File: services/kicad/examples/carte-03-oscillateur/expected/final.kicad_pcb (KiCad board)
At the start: 2 copper layers, 26 x 20 mm, 15 parts, among them J1 PWR, J2 OUT, U1 NE555

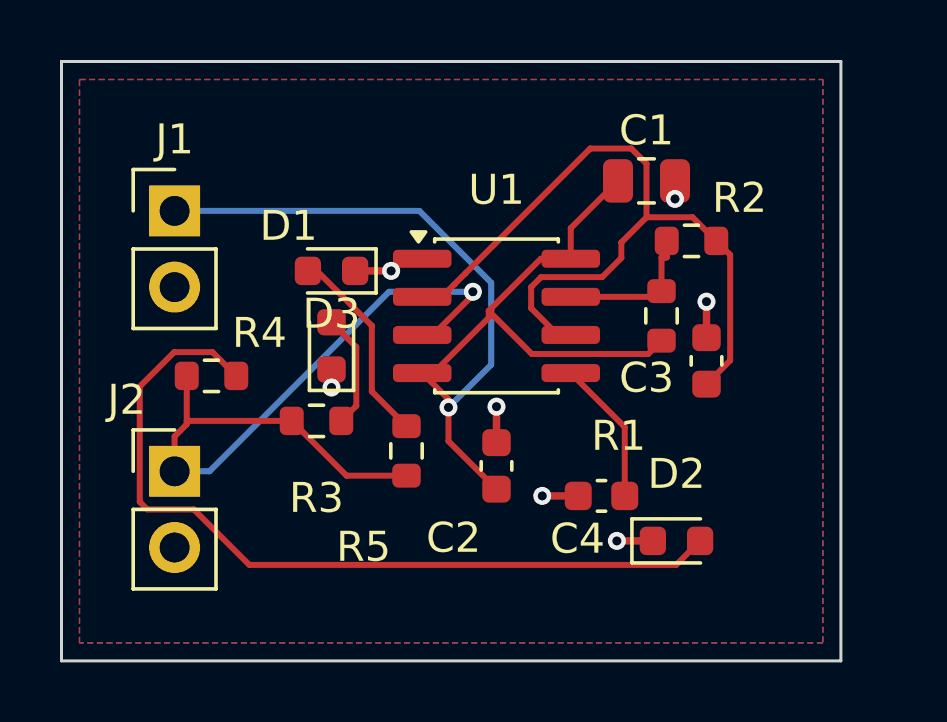
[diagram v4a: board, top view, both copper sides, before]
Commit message: feat(placement): les peripheriques se REPARTISSENT, ils ne s empilent plus
Question de l utilisateur devant le rendu : « c est quoi ce type de placement ? ».
Les composants s entassaient d un seul cote du boitier, etiquettes de
serigraphie l une sur l autre, trois quarts de la couronne vides.

TROIS CAUSES, toutes dans `_poser_les_peripheriques`, toutes la meme faute —
un angle unique pour tout un groupe :

  - les DIRECTS qui visent la meme broche (tous les decouplages d un rail,
    toutes les resistances d un meme signal) recevaient le MEME `angle_vers`
    et le meme rayon de depart ;
  - les SUIVEURS d un meme parent recevaient tous atan2(parent - centre) ;
  - les ISOLES partaient tous de l angle 0.0, c est-a-dire du meme point.

`le_long_du_rayon` ne s ecartait qu une fois la place prise : d ou la file.

REMEDE : `_ecart_en_eventail`. Le PREMIER de chaque groupe garde EXACTEMENT la
direction calculee — c est la topologie, on ne la perd pas pour faire joli — et
les suivants s ecartent symetriquement de 3 x `_PAS_ANGLE_DEG`.
Rien de deja pose ne bouge : seul l ANGLE DE DEPART de la recherche change, et
`le_long_du_rayon` reste seul juge de ce qui est libre.

BANC DES DIX CARTES, contour resserre ET peripheriques repartis :

    carte             demandee    livree         err  manq
    carte-01           25 x 20    20,1 x 13,6     0    0
    carte-02           55 x 40    34,9 x 25,2     0    0
    carte-03           50 x 35    27,6 x 19,9     0    0
    carte-04           60 x 45    36,6 x 29,8     0    0
    carte-05           70 x 50    40,0 x 32,6     0    0
    carte-06           80 x 60    46,5 x 36,4     0    0
    carte-07          110 x 80    47,7 x 38,8     0    0
    carte-08          125 x 95    57,4 x 44,1     0    0
    carte-09          130 x 100   57,8 x 45,2     0    0
    carte-10          140 x 105   59,0 x 45,8     0    0

Dix sur dix, 100 % route. carte-07 gagne 5,5 mm de largeur sur le passage
precedent, carte-06 deux, carte-10 deux. Sur ca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
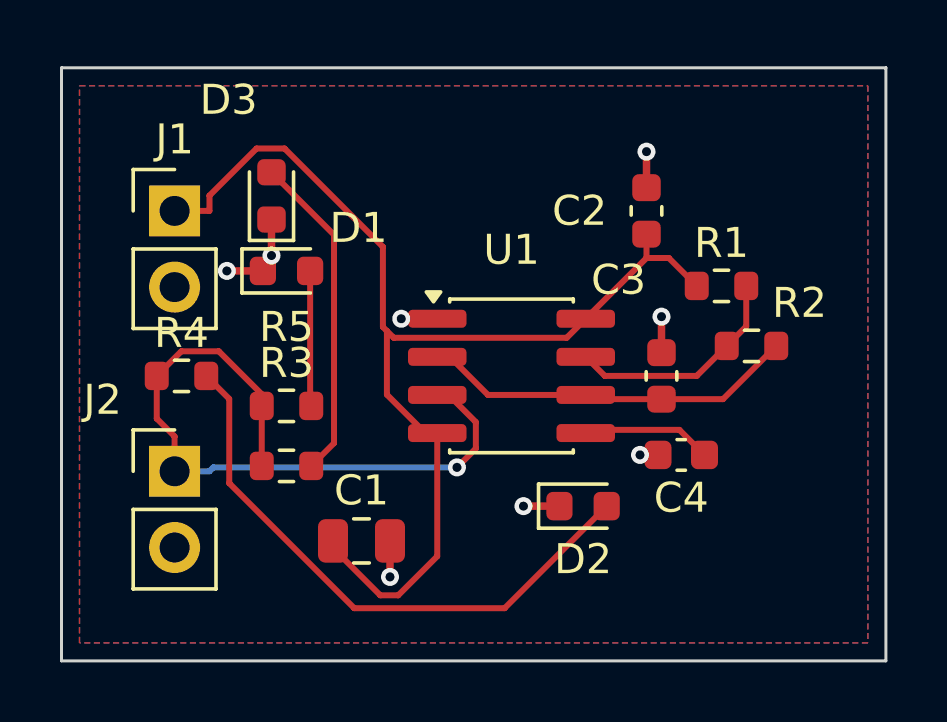
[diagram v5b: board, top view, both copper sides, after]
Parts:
- moved C1 15.3 mm to (133.5, 103.5)
- moved C2 9.86 mm to (143.0, 92.5)
- moved R2 4.03 mm to (146.5, 97.0)
- moved R5 4.03 mm to (131.0, 101.0), turned to 0 degrees
- moved D2 3.32 mm to (140.9, 102.3)
- moved D3 3.20 mm to (130.5, 92.0), turned to 90 degrees
- moved C4 2.99 mm to (144.2, 100.6)
- moved D1 2.92 mm to (131.0, 94.5), turned to 0 degrees
- moved R1 2.24 mm to (145.5, 95.0), turned to 0 degrees
- moved U1 2.06 mm to (138.5, 98.0)
- moved C3 1.58 mm to (143.5, 98.0)
- moved R3 1.12 mm to (131.0, 99.0)
- moved R4 1.00 mm to (127.5, 98.0)
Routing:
- net THRES: track 27.0 -> 12.6 mm
- net LED2_A: track 27.7 -> 19.6 mm
- net LED3_A: track 6.71 -> 11.0 mm
- net OUT: track 26.2 -> 23.1 mm
- net DISCH: track 4.95 -> 7.65 mm
- net GND: track 7.20 -> 9.00 mm, vias 7 -> 8
- net VCC: track 37.5 -> 38.4 mm, vias 1 -> 0
- net LED1_A: track 3.84 -> 4.52 mm
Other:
- board size 26 x 20 mm -> 27.5 x 19.8 mm

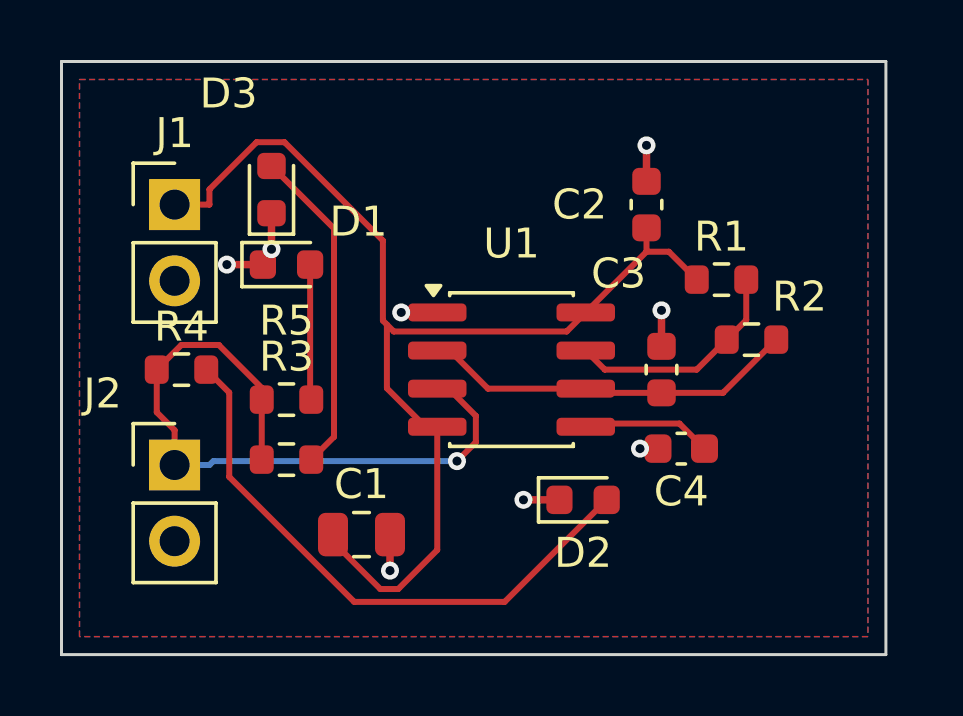
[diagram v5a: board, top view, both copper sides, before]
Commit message: docs(banc): les dix boards du banc du 2026-09-23, service corrige
Artefacts du banc dont le tableau est deja commite : les dix cartes a
100 % route, 0 erreur, 0 connexion manquante, chacune a la taille de son
circuit.

Co-Authored-By: Claude Opus 5 <noreply@anthropic.com>
Claude-Session: https://claude.ai/code/session_01TnMqm4La2CxQHHB5K8aSSV
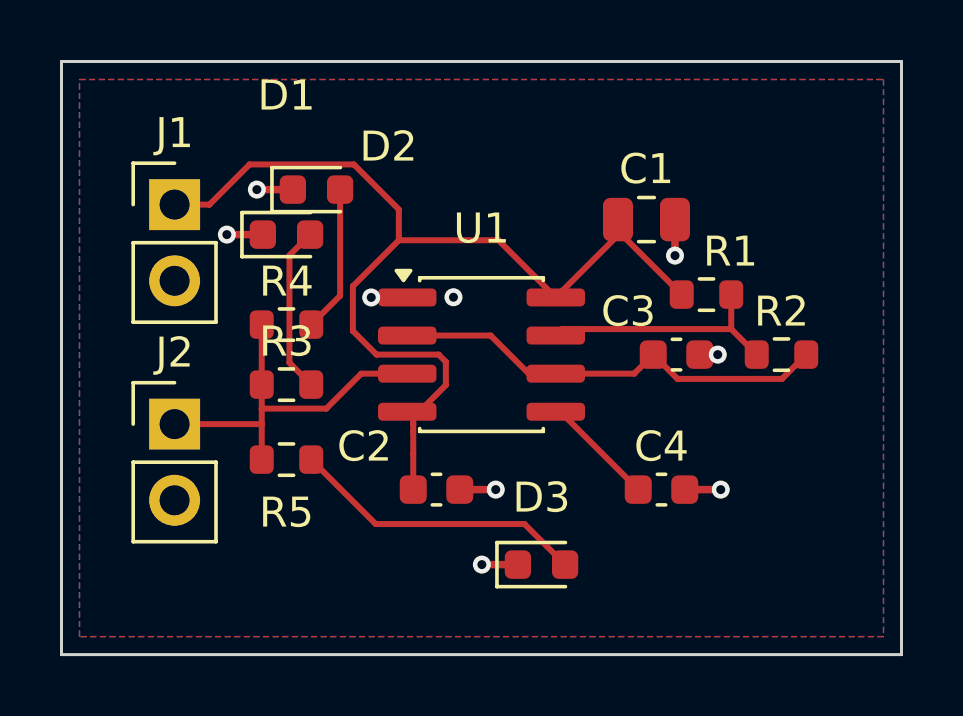
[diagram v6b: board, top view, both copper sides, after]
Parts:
- moved D3 15.4 mm to (139.5, 104.5), turned to 0 degrees
- moved C1 14.2 mm to (143.0, 93.0)
- moved D2 13.6 mm to (132.0, 92.0)
- moved C2 11.8 mm to (136.0, 102.0), turned to 0 degrees
- moved R4 3.81 mm to (131.0, 96.5)
- moved C4 1.52 mm to (143.5, 102.0), turned to 0 degrees
- moved J2 1.36 mm to (127.3, 99.8)
- moved R2 1.12 mm to (147.5, 97.5)
- moved U1 1.12 mm to (137.5, 97.5)
- moved D1 1.00 mm to (131.0, 93.5)
- moved C3 0.71 mm to (144.0, 97.5), turned to 0 degrees
- moved R1 0.71 mm to (145.0, 95.5)
- moved R3 0.50 mm to (131.0, 98.5)
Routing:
- net LED2_A: track 19.6 -> 4.90 mm
- net OUT: track 23.1 -> 12.7 mm, vias 1 -> 0
- net VCC: track 38.4 -> 34.3 mm
- net THRES: track 12.6 -> 14.8 mm
- net LED1_A: track 4.52 -> 5.59 mm
- net LED3_A: track 11.0 -> 9.91 mm
- net DISCH: track 7.65 -> 8.29 mm
- net CTRL: track 4.35 -> 3.82 mm
- net GND: vias 8 -> 9
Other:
- board size 27.5 x 19.8 mm -> 28 x 19.8 mm
